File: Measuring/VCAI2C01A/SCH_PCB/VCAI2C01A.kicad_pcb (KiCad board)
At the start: 2 copper layers, 60.5 x 40.1 mm, 74 parts, among them J10 JUMP2_2x1, J11 JUMP2_2x1, J13 JUMP_5X2, J14 JUMP_2x1, J15 JUMP_2x1, J16 JUMP_2x1, J17 JUMP_2x1, J18 JUMP_2x1, J19 JUMP_2x1, J2 CONN_2, J20 JUMP_2x1, J21 JUMP_2x1, J22 JUMP_2x1, J23 JUMP_2x1, J3 JUMP_2x1, J4 CONN_2, J5 JUMP_2x1, J6 CONN_2, J7 JUMP_2x1, J8 CONN_2, J9 JUMP_2x1, M1 HOLE, M2 HOLE, M3 HOLE, M4 HOLE, U1 TLC27L2ID, U2 TLC27L2ID, U3 MCP3424

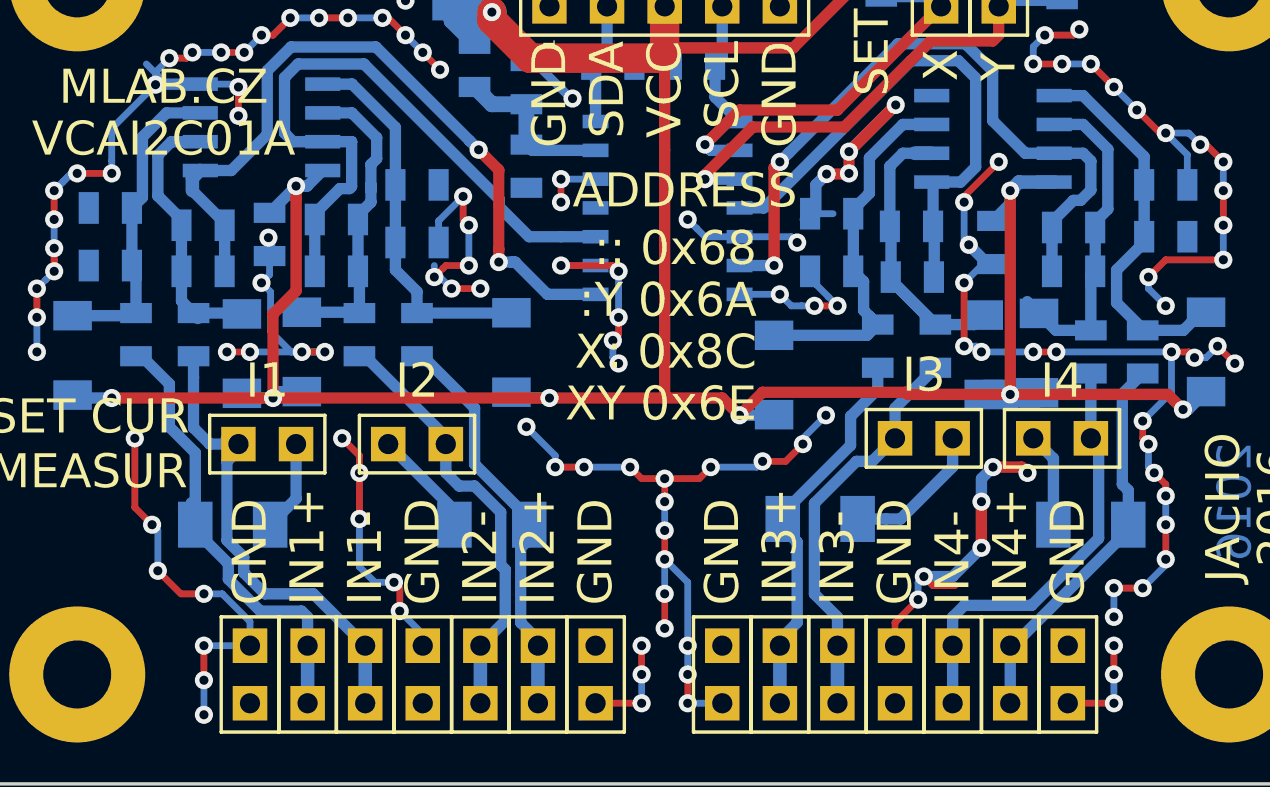
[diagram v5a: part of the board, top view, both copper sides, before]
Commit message: 
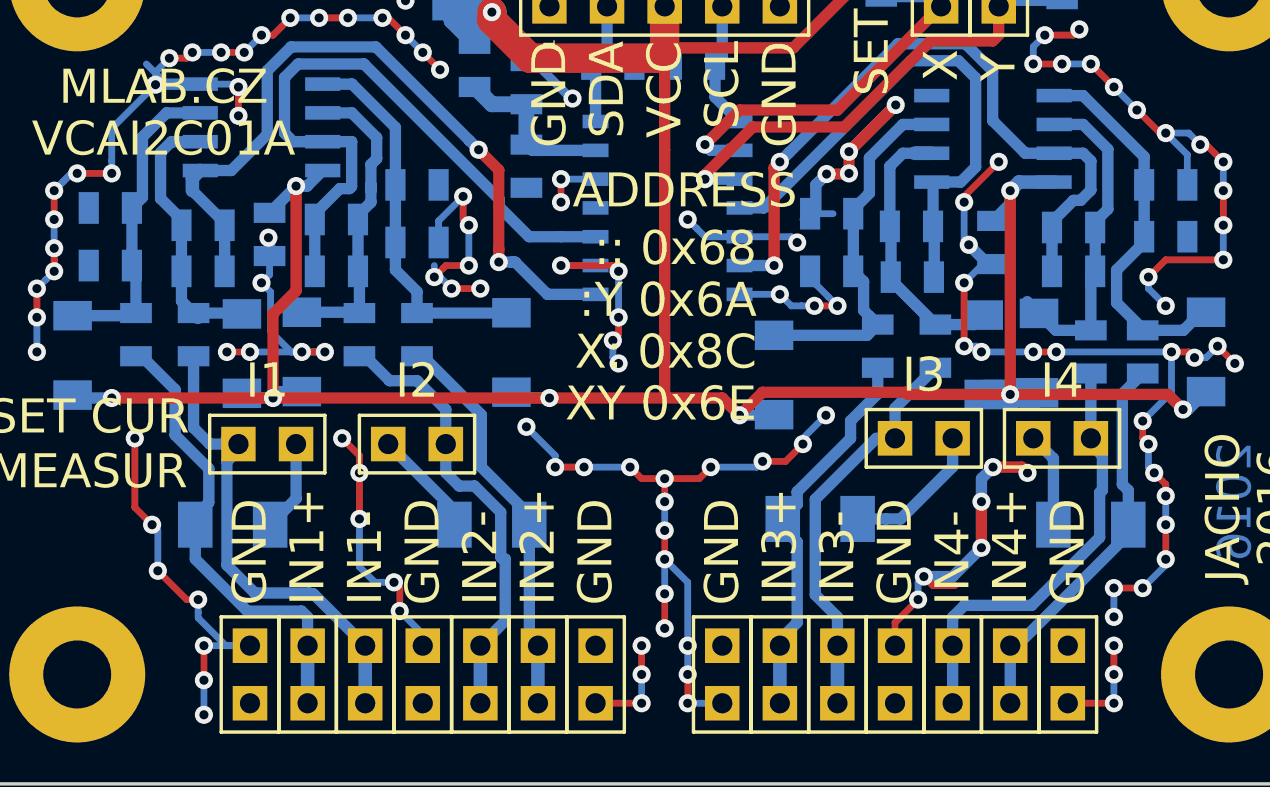
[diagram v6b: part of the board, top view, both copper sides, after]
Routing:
- net /IN1+: track 22.6 -> 21.1 mm
- net /IN2-: track 19.0 -> 19.7 mm

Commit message: 
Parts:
- C1, C10, C11, C4, C6, C7, C8, C9: value C -> 10nF
